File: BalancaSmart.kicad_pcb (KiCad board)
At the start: 2 copper layers, 100 x 100 mm, 25 parts, among them J1 Load Cell, J2 NeoPixel Ring Light, Q1 IRF9540N, Q4 S8050, SW1 SW_Push, U1 HX711-Mod, U2 ADS1115-module, U3 HX-2S-JH20, U4 XL4015, U5 Optocoupler_DC_PhotoNPN_AKEC

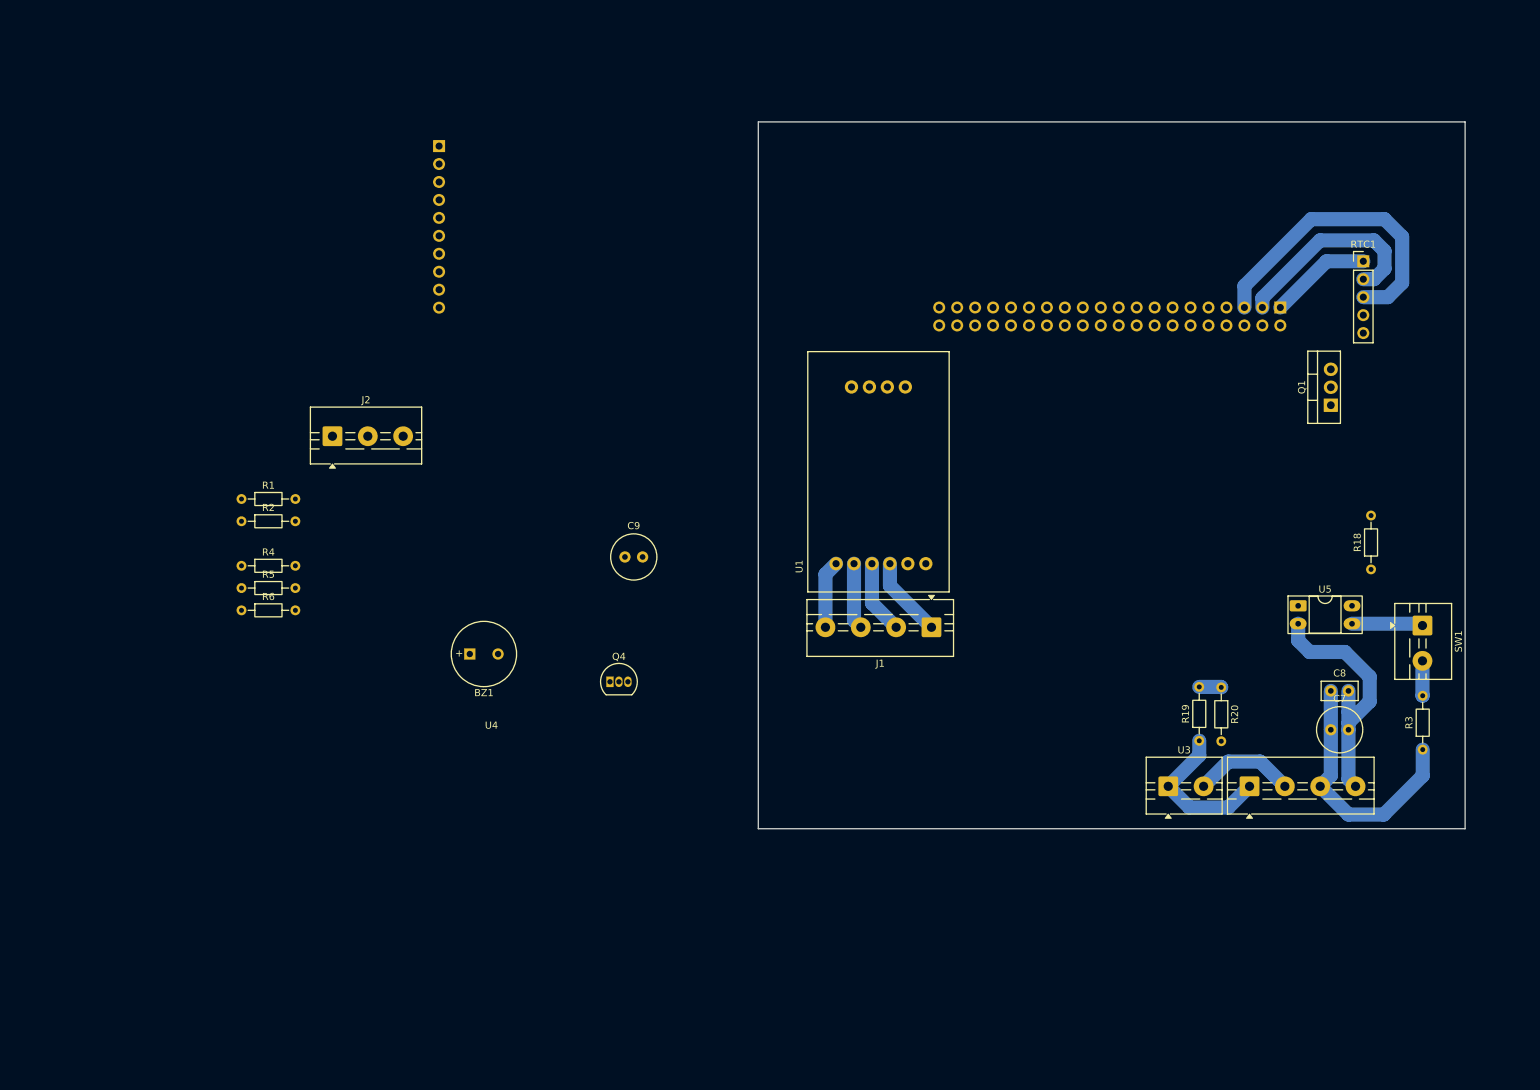
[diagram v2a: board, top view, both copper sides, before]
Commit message: alteração no circuito de liga/desliga
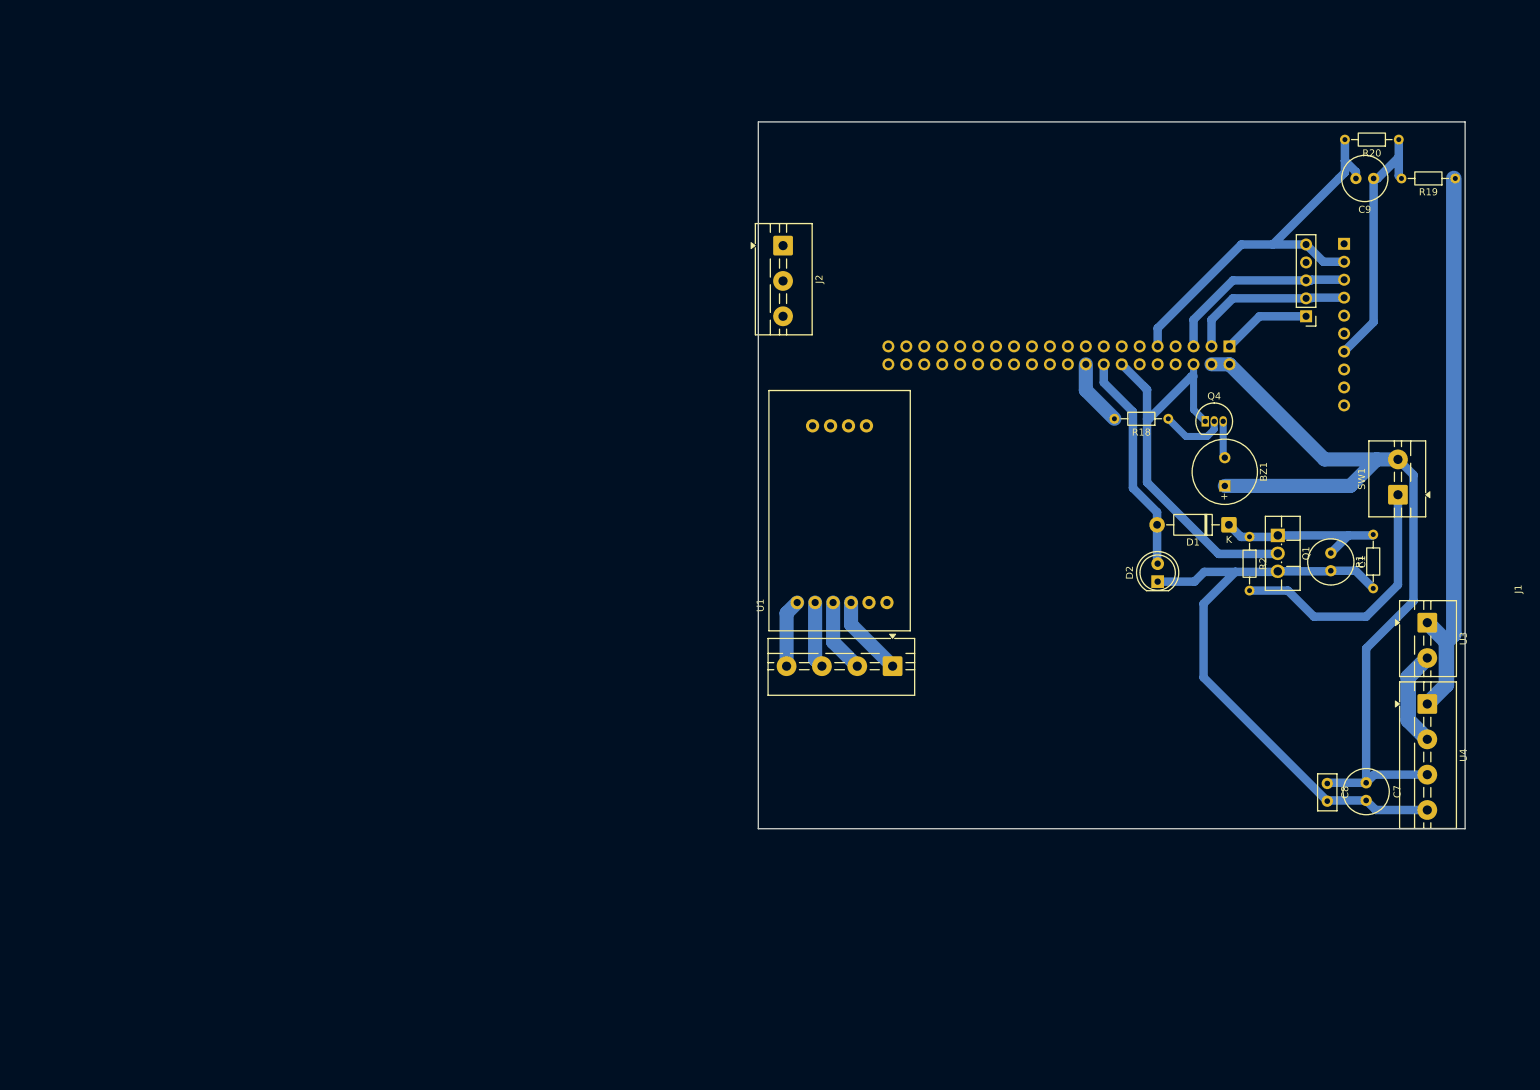
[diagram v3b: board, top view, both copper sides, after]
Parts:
- removed R3, R4, R6: 1k, Resistor_THT:R_Axial_DIN0204_L3.6mm_D1.6mm_P7.62mm_Horizontal
- removed R5: 2k, Resistor_THT:R_Axial_DIN0204_L3.6mm_D1.6mm_P7.62mm_Horizontal
- removed U5: Optocoupler_DC_PhotoNPN_AKEC, Package_DIP:DIP-4_W7.62mm_Socket_LongPads
- added C1: 470uF, Capacitor_THT:C_Radial_D6.3mm_H7.0mm_P2.50mm, F.Cu at (248.5, 102.0)
- added D1: 1N4007, Diode_THT:D_DO-41_SOD81_P10.16mm_Horizontal, F.Cu at (234.1, 98.0)
- added D2: LED, LED_THT:LED_D5.0mm, F.Cu at (224.0, 106.0)
- Q1: value IRF9540N -> IRLIZ44N; footprint Package_TO_SOT_THT:TO-220-3_Vertical -> Package_TO_SOT_THT:TO-220F-3_Vertical
- R1: value 1M -> 10kR
- R2: value 100k -> 220R
- moved R1 160.6 mm to (254.5, 107.0), turned to 90 degrees
- moved R2 142.6 mm to (237.0, 99.7), turned to -90 degrees
- moved U2 128.8 mm to (257.0, 51.0)
- moved C9 118.7 mm to (254.6, 49.0), turned to 180 degrees
- moved BZ1 109.4 mm to (233.5, 92.5), turned to 90 degrees
- moved Q4 91.9 mm to (230.7, 83.4)
- moved R19 87.4 mm to (266.1, 49.0), turned to 180 degrees
- moved R20 81.5 mm to (258.1, 43.5), turned to 180 degrees
- moved J2 69.2 mm to (171.0, 58.5), turned to -90 degrees
- moved U3 43.3 mm to (262.1, 111.8), turned to -90 degrees
- moved R18 35.7 mm to (225.5, 83.0), turned to 180 degrees
- moved U4 27.7 mm to (262.1, 123.3), turned to -90 degrees
- moved Q1 19.9 mm to (241.0, 99.5), turned to -90 degrees
- moved SW1 18.8 mm to (258.0, 93.8), turned to 90 degrees
- moved C8 13.1 mm to (248.0, 134.6), turned to -90 degrees
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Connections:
- A1 pad 11: Ring Light -> unconnected-(A1-GP17-Pad11)
- A1 pad 14: (no net) -> Earth
- A1 pad 16: unconnected-(A1-GP23-Pad16) -> power holding
- A1 pad 18: unconnected-(A1-GP24-Pad18) -> Buzzer
- A1 pad 2: pino 5v rasp -> +5V
- A1 pad 20: (no net) -> Earth
- A1 pad 25: (no net) -> unconnected-(A1-GND-Pad25)
- A1 pad 30: (no net) -> unconnected-(A1-GND-Pad30)
- A1 pad 32: Controle LEDs -> Ring Light
- A1 pad 34: (no net) -> Earth
- A1 pad 35: button pin -> unconnected-(A1-GP19-Pad35)
- A1 pad 39: (no net) -> Earth
- A1 pad 4: pino 5v rasp -> +5V
- A1 pad 40: Buzzer -> unconnected-(A1-GP21-Pad40)
- A1 pad 7: Sinal de desligamento -> unconnected-(A1-GP4-Pad7)
- A1 pad 9: (no net) -> Earth
- BZ1 pad 1: pino 5v rasp -> +5V
- C7 pad 2: Earth -> GND
- C8 pad 2: Earth -> GND
- Q1 pad 2: +5V -> Earth
- Q1 pad 3: pino 5v rasp -> GND
- R1 pad 1: +5V -> GND
- SW1 pad 1: Earth -> Net-(R2-Pad2)
- SW1 pad 2: Net-(R2-Pad2) -> +5V
- U1 pad 7: pino 5v rasp -> +5V
- U4 pad 4: Earth -> GND
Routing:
- net GND: track 0.00 -> 88.5 mm
- net +5V: track 36.2 -> 119.1 mm
- net Earth: track 46.3 -> 116.6 mm
- net P+: track 22.2 -> 79.7 mm
- net Net-(U2-A0): track 3.14 -> 36.7 mm
- net Net-(R2-Pad2): track 4.95 -> 37.1 mm
- net power holding: track 0.00 -> 31.4 mm
- net Net-(D1-K): track 0.00 -> 24.8 mm
- net I2C SCL: track 43.2 -> 27.4 mm
- net Buzzer: track 0.00 -> 9.38 mm
- net Net-(Q4-B): track 0.00 -> 9.09 mm
- net Net-(BZ1--): track 0.00 -> 5.24 mm
- net I2C SDA: track 28.7 -> 24.5 mm
- net +3V3: track 14.4 -> 12.6 mm
- net P-: track 14.4 -> 13.7 mm

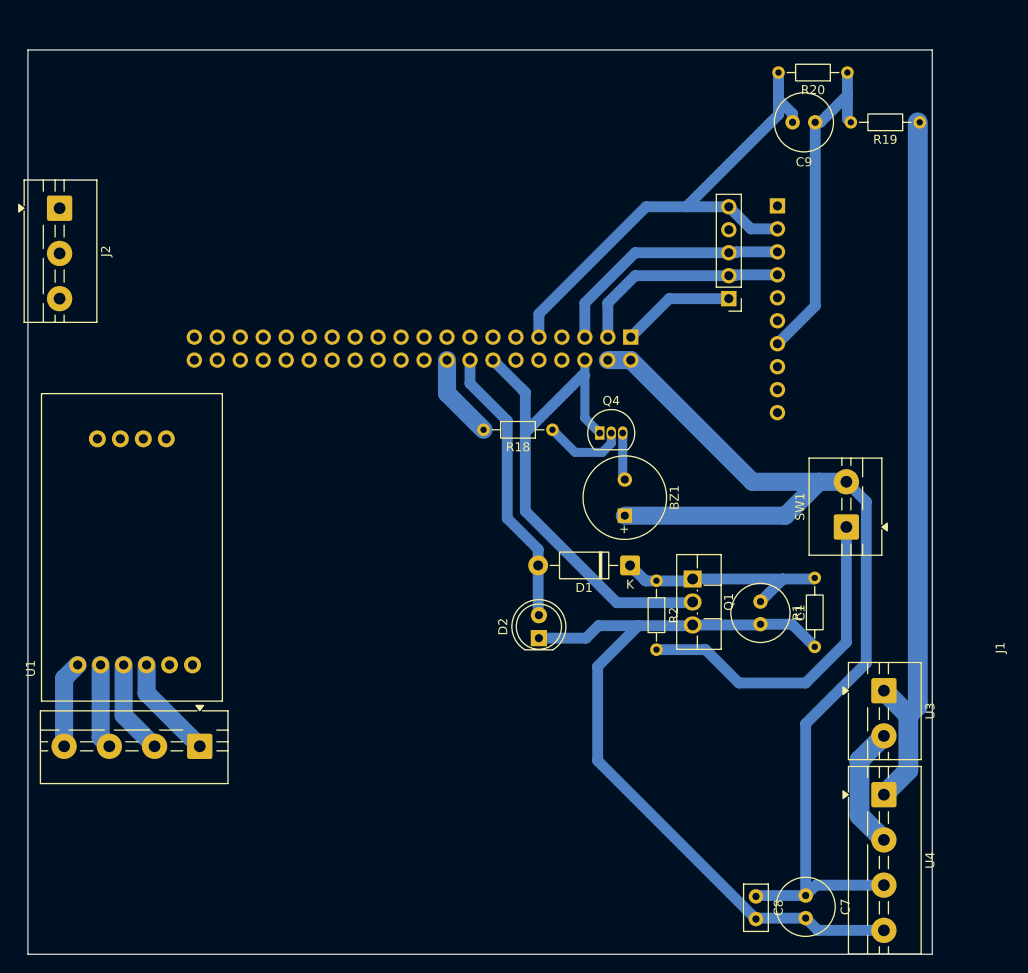
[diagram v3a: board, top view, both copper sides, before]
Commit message: adicionado resistor para a ring light e refeitas as rotas (tudo roteado corretamente)
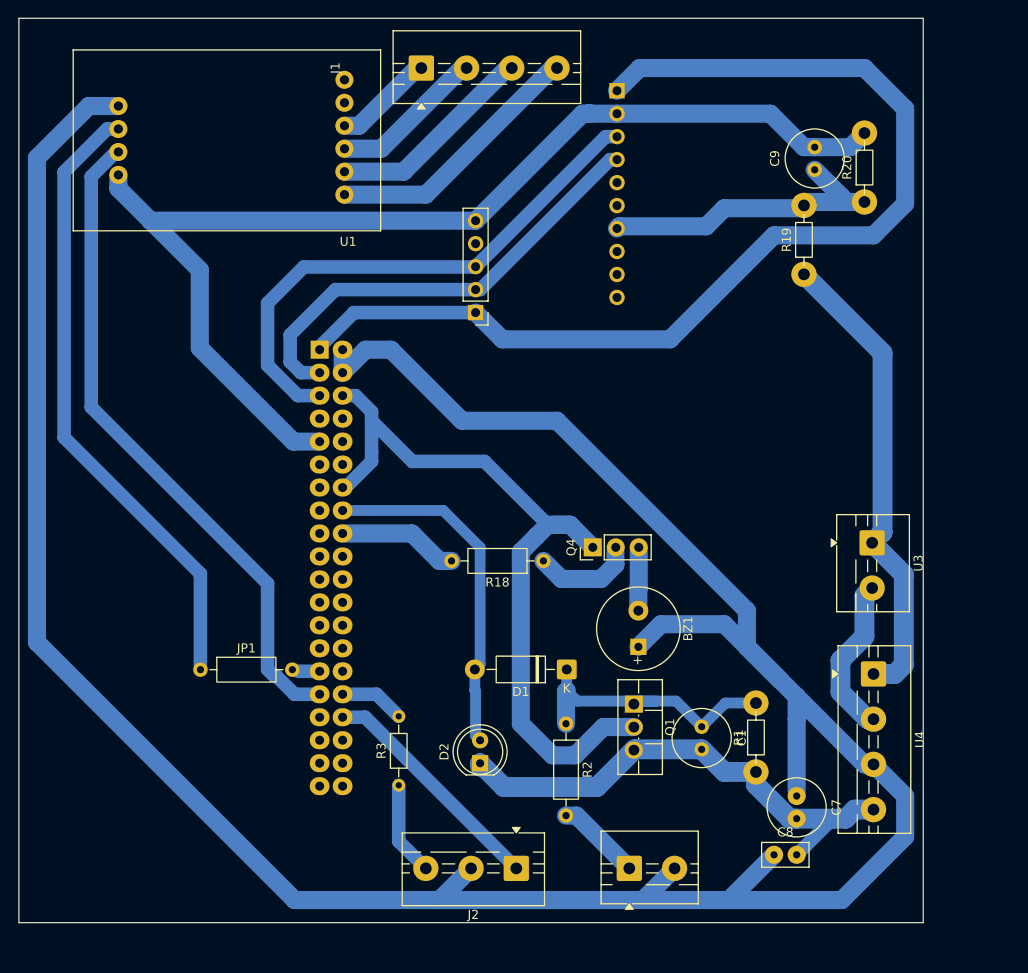
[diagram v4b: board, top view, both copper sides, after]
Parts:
- added JP1: Jumper, Resistor_THT:R_Axial_DIN0207_L6.3mm_D2.5mm_P10.16mm_Horizontal, F.Cu at (186.6, 109.5)
- added R3: 470, Resistor_THT:R_Axial_DIN0204_L3.6mm_D1.6mm_P7.62mm_Horizontal, F.Cu at (208.5, 122.3)
- Q4: footprint Package_TO_SOT_THT:TO-92_Inline -> Connector_PinHeader_2.54mm:PinHeader_1x03_P2.54mm_Vertical
- R18, R2: footprint Resistor_THT:R_Axial_DIN0204_L3.6mm_D1.6mm_P7.62mm_Horizontal -> Resistor_THT:R_Axial_DIN0207_L6.3mm_D2.5mm_P10.16mm_Horizontal
- moved J2 88.8 mm to (221.5, 131.5), turned to 180 degrees
- moved J1 78.9 mm to (211.0, 43.0), turned to 0 degrees
- moved U1 46.2 mm to (189.5, 51.0), turned to 180 degrees
- moved SW1 44.7 mm to (234.0, 131.5), turned to 0 degrees
- moved A1 34.4 mm to (199.8, 74.1), turned to 180 degrees
- moved RTC1 28.0 mm to (217.0, 70.0)
- moved U2 21.8 mm to (239.3, 38.3)
- moved R19 21.1 mm to (253.3, 65.8), turned to 90 degrees
- moved R2 18.7 mm to (227.0, 115.5)
- moved U3 16.4 mm to (260.9, 95.5)
- moved C1 15.3 mm to (242.0, 115.8)
- moved D2 15.3 mm to (217.5, 119.9)
- moved Q1 15.3 mm to (234.5, 113.3)
- moved R1 15.3 mm to (248.0, 120.8)
- moved BZ1 14.6 mm to (235.0, 107.0)
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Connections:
- J2 pad 2: pino 5v rasp -> +5V
- J2 pad 3: Ring Light -> Net-(J2-Pin_3)
- U1 pad 8: CLK HX711 -> Net-(JP1-A)
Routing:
- net +5V: track 119.1 -> 316.1 mm
- net Earth: track 116.6 -> 237.2 mm
- net +3V3: track 12.6 -> 119.3 mm
- net DAT HX711: track 0.00 -> 73.6 mm
- net Net-(JP1-A): track 0.00 -> 69.2 mm
- net I2C SCL: track 27.4 -> 60.3 mm
- net Net-(R2-Pad2): track 37.1 -> 9.42 mm
- net P+: track 79.7 -> 52.5 mm
- net GND: track 88.5 -> 61.4 mm
- net I2C SDA: track 24.5 -> 50.9 mm
- net Net-(J1-Pin_4): track 9.62 -> 29.3 mm
- net Net-(J1-Pin_3): track 9.40 -> 23.2 mm
- net Net-(J2-Pin_3): track 0.00 -> 10.4 mm
- net Net-(D1-K): track 24.8 -> 32.3 mm
- net power holding: track 31.4 -> 38.7 mm
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
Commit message: adiciona borne para o display
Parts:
- added J3: Display, TerminalBlock:TerminalBlock_MaiXu_MX126-5.0-02P_1x02_P5.00mm, F.Cu at (256.5, 82.0)
- moved R20 0.39 mm to (259.9, 58.2)
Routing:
- net +5V: track 316.1 -> 363.4 mm
- net Earth: track 237.2 -> 283.9 mm
- net GND: track 61.4 -> 67.2 mm
- net DAT HX711: track 73.6 -> 74.5 mm
- net P-: track 17.8 -> 18.5 mm
- net P+: track 52.5 -> 53.2 mm
